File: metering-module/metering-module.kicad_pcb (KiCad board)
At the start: 2 copper layers, 86 x 31 mm, 36 parts, among them J1 North, J2 South, J3 West, J4 East, Q1 MMBT3904, Q2 MMBT3904, U1 LTV-817S, U2 LTV-817S, U3 BA033CC0FP-E2, U4 MAX3486, U5 MAX3486, U6 MCP23008-xSO

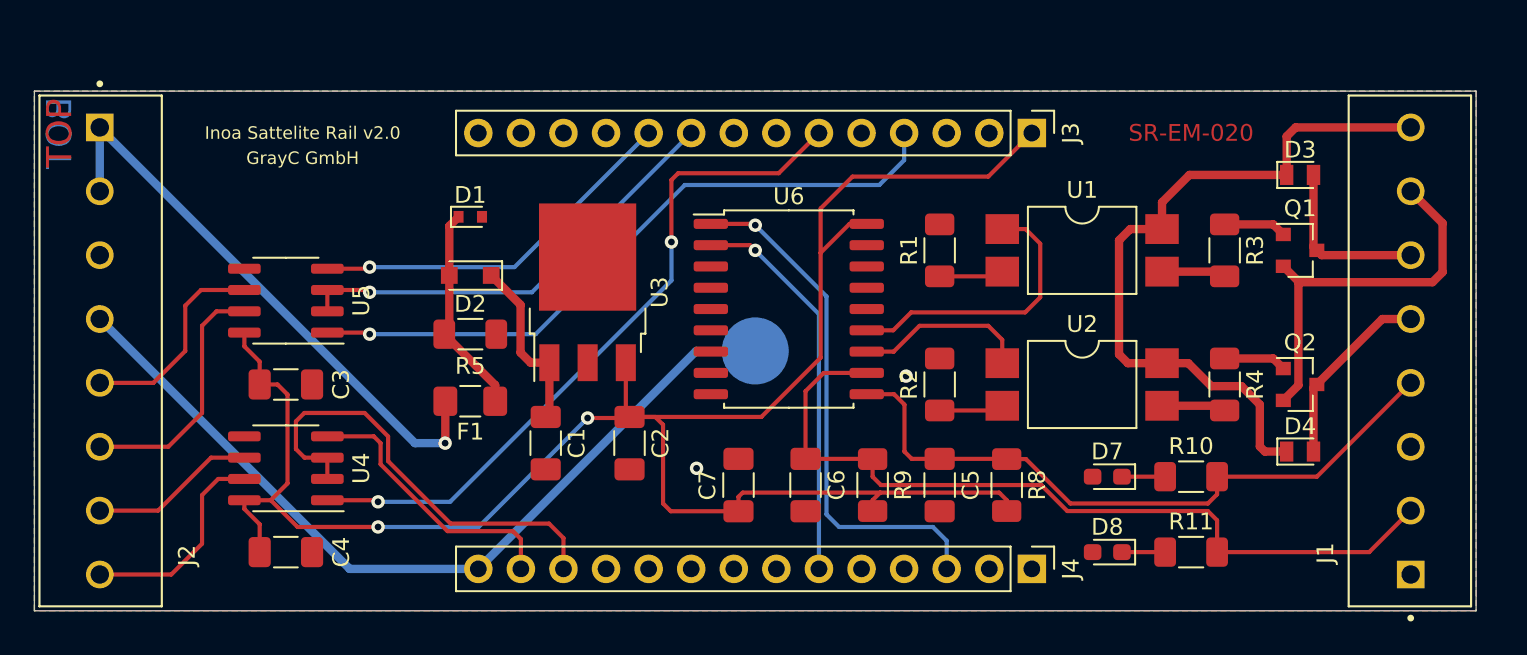
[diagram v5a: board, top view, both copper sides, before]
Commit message: Work on Ethernet module
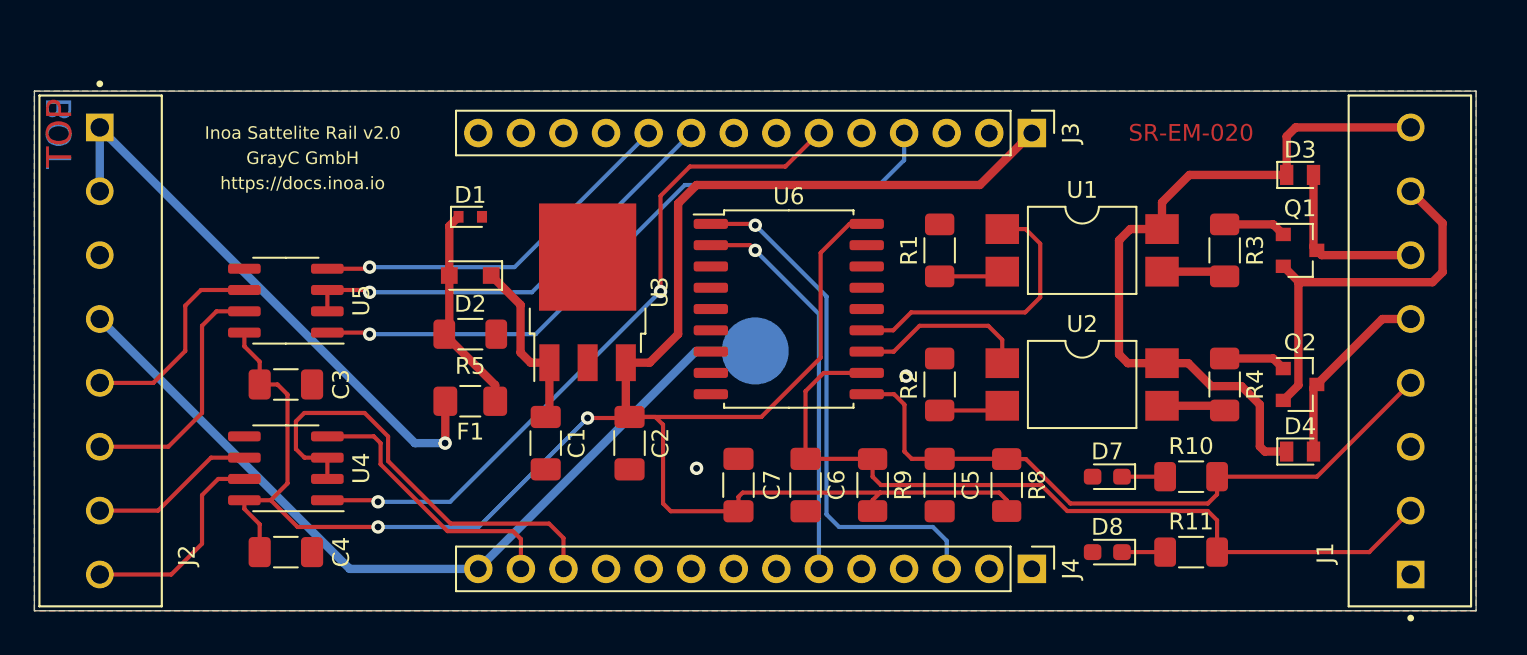
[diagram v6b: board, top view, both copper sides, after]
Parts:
- added G1: LOGO, images:grayc-logo-negative, B.Cu at (174.4, 107.5)
- C1: value 100nF / 30V -> 100nF / 35V
- F1: value Fuse -> 25V/1A
- R1, R10, R11, R2: value R -> 220R
- R3, R4: value R -> 1k
- R8, R9: value R -> 10k
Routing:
- net +3V3: track 115.8 -> 133.2 mm
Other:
- board text added: "https://docs.inoa.io"

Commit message: Added metering module to CI build
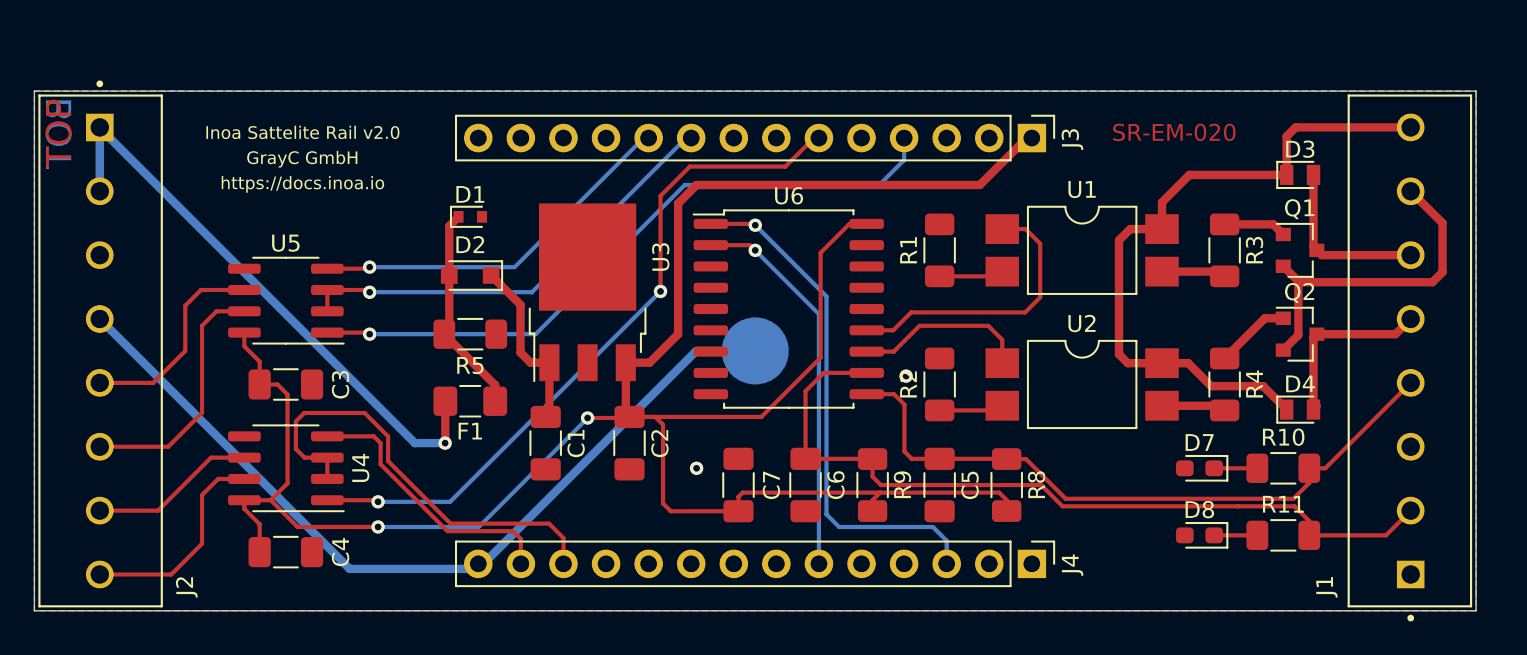
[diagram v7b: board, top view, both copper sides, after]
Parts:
- moved G1 63.0 mm to (116.0, 84.0)
- moved D8 5.59 mm to (169.5, 106.5)
- moved R11 5.59 mm to (174.5, 106.5)
- moved D7 5.52 mm to (169.5, 102.5)
- moved R10 5.52 mm to (174.5, 102.5)
- moved Q2 3.00 mm to (175.5, 94.5)
- moved D4 2.50 mm to (175.5, 99.0)
- moved J3 0.30 mm to (159.5, 82.8)
- moved J4 0.30 mm to (159.5, 108.2)
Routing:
- net GND1: track 23.2 -> 20.2 mm
- net VS: track 43.1 -> 40.6 mm
- net S0_1: track 49.3 -> 47.9 mm
- net Net-(Q2-Pad1): track 3.75 -> 4.49 mm

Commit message: Fix Footprint of MCP23009
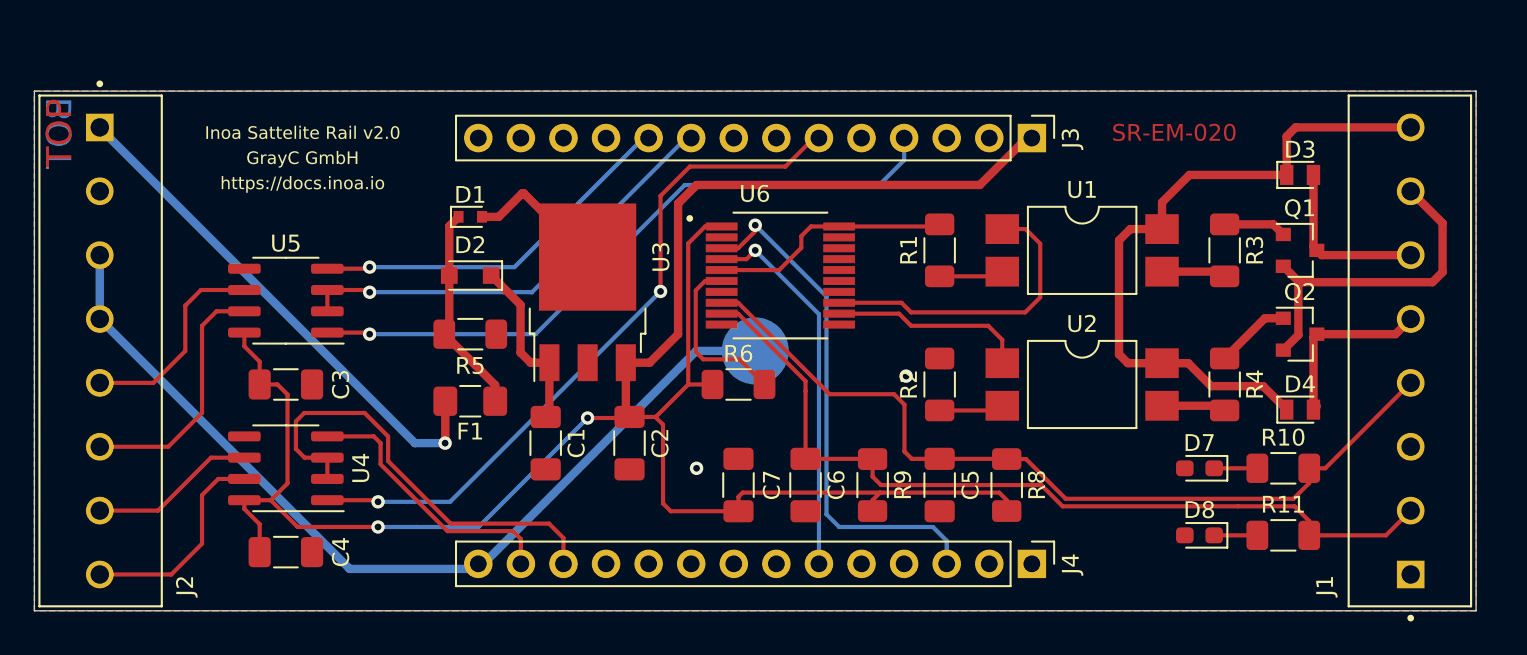
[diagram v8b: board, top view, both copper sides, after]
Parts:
- added R6: 0R, Resistor_SMD:R_1206_3216Metric_Pad1.30x1.75mm_HandSolder, F.Cu at (142.0, 97.5)
- U6: value MCP23008-xSO -> MCP23009-E_SS; footprint Package_SO:SOIC-18W_7.5x11.6mm_P1.27mm -> footprints:SOP65P780X200-20N
- moved U6 2.06 mm to (144.5, 91.0)
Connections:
- J2 pad 2: VCC -> GND
- J2 pad 3: GND -> GNDPWR
- J3 pad 11: Net-(J3-Pad11) -> (no net)
- J3 pad 12: Net-(J3-Pad12) -> (no net)
- J3 pad 13: Net-(J3-Pad13) -> (no net)
- J3 pad 14: Net-(J3-Pad14) -> (no net)
- J3 pad 2: Net-(J3-Pad2) -> (no net)
- J3 pad 3: Net-(J3-Pad3) -> (no net)
- J3 pad 5: Net-(J3-Pad5) -> (no net)
- J3 pad 7: Net-(J3-Pad7) -> (no net)
- J3 pad 8: Net-(J3-Pad8) -> (no net)
- J4 pad 10: Net-(J4-Pad10) -> (no net)
- J4 pad 11: Net-(J4-Pad11) -> (no net)
- J4 pad 2: Net-(J4-Pad2) -> (no net)
- J4 pad 4: Net-(J4-Pad4) -> (no net)
- J4 pad 5: Net-(J4-Pad5) -> (no net)
- J4 pad 7: Net-(J4-Pad7) -> (no net)
- J4 pad 8: Net-(J4-Pad8) -> (no net)
- J4 pad 9: Net-(J4-Pad9) -> (no net)
- U6 pad 1: I2C_SCL -> +3V3
- U6 pad 10: S0_0 -> (no net)
- U6 pad 11: S0_1 -> (no net)
- U6 pad 14: Net-(U6-Pad14) -> (no net)
- U6 pad 15: Net-(U6-Pad15) -> (no net)
- U6 pad 16: Net-(U6-Pad16) -> (no net)
- U6 pad 17: Net-(U6-Pad17) -> (no net)
- U6 pad 18: +3V3 -> (no net)
- U6 pad 2: I2C_SDA -> (no net)
- U6 pad 3: GND -> I2C_SCL
- U6 pad 4: GND -> I2C_SDA
- U6 pad 6: Net-(U6-Pad6) -> IO_RESET
- U6 pad 7: Net-(U6-Pad7) -> (no net)
- U6 pad 8: S0_INT -> S0_0
- U6 pad 9: GND -> S0_1
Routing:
- net GND: track 0.00 -> 23.0 mm
- net S0_0: track 40.1 -> 51.0 mm
- net IO_RESET: track 0.00 -> 10.3 mm
- net +3V3: track 133.2 -> 125.6 mm
- net GNDPWR: track 50.7 -> 54.5 mm
- net VCC: track 34.7 -> 30.9 mm
- net S0_1: track 47.9 -> 51.1 mm
- net SW0: track 17.0 -> 18.4 mm
- net SW1: track 10.5 -> 11.8 mm
- net I2C_SDA: track 23.4 -> 22.8 mm
